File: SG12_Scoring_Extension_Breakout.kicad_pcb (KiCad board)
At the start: 2 copper layers, 100 x 100 mm, 37 parts, among them J1 RJ45, J10 Conn_01x02, J11 Conn_01x02, J12 Conn_01x02, J13 Conn_01x02, J14 Conn_01x02, J15 Conn_01x02, J16 Conn_02x04_Top_Bottom, J17 Conn_02x04_Top_Bottom, J18 Conn_02x04_Top_Bottom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

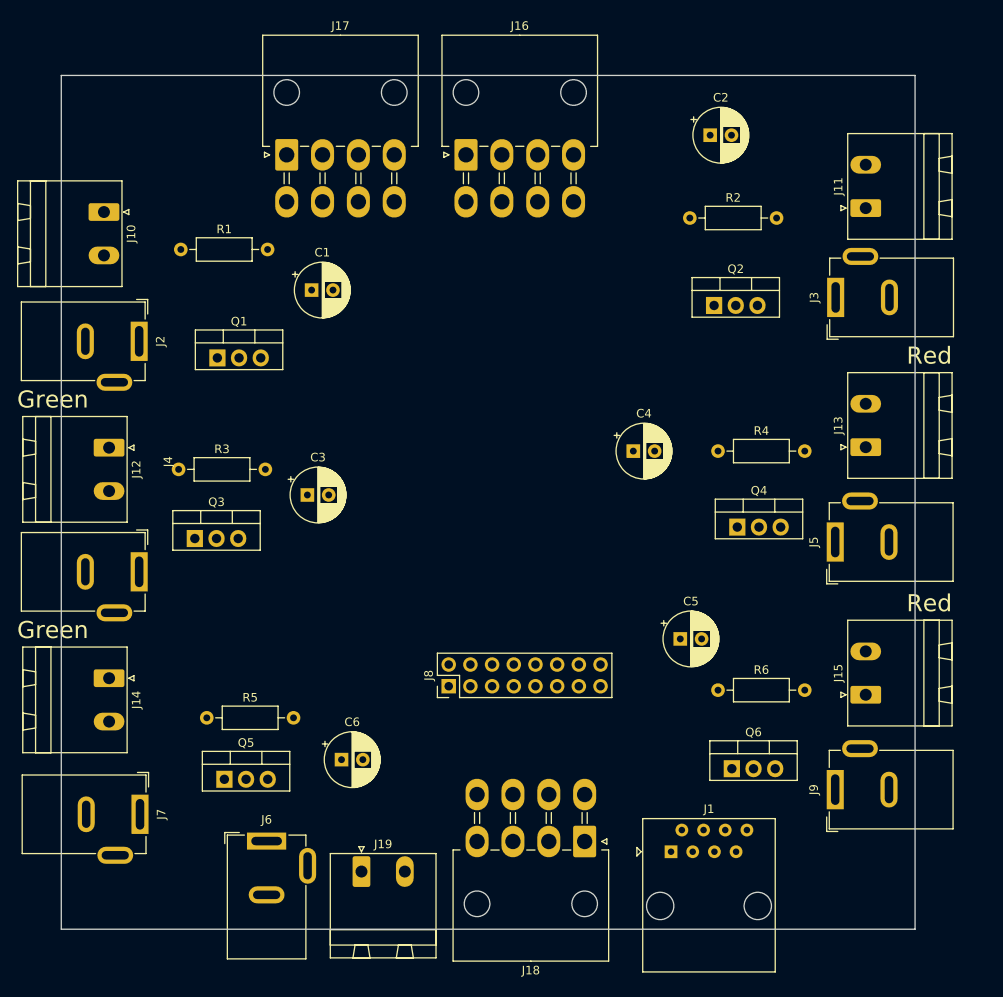
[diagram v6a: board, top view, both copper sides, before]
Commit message: Added mouting holes, iteration 2
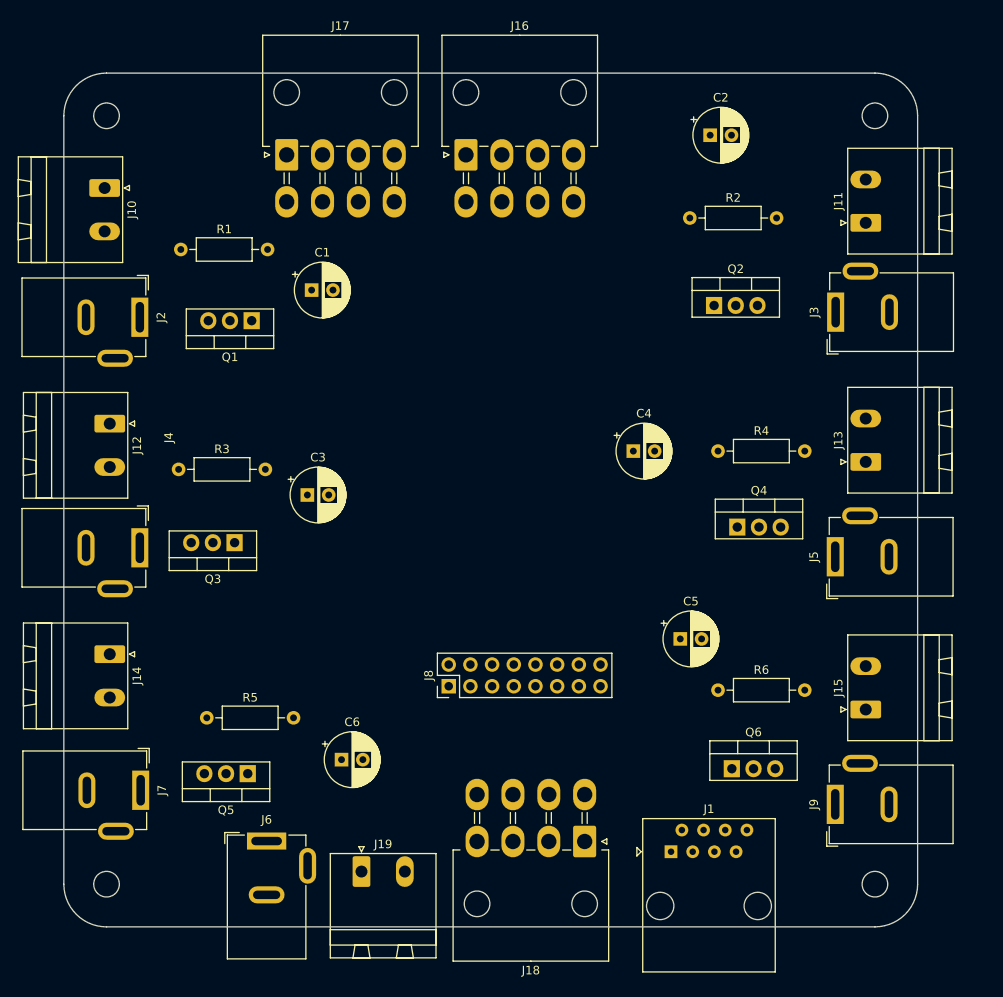
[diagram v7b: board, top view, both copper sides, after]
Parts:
- added REF**: MountingHole_3mm, MountingHole:MountingHole_3mm, F.Cu at (198.0, 53.0)
- added REF**: MountingHole_3mm, MountingHole:MountingHole_3mm, F.Cu at (108.0, 53.0)
- added REF**: MountingHole_3mm, MountingHole:MountingHole_3mm, F.Cu at (108.0, 143.0)
- added REF**: MountingHole_3mm, MountingHole:MountingHole_3mm, F.Cu at (198.0, 143.0)
- moved Q1 5.93 mm to (125.0, 77.0), turned to 180 degrees
- moved Q3 4.68 mm to (123.0, 103.0), turned to 180 degrees
- moved J2 2.82 mm to (111.9, 76.6)
- moved J4 2.82 mm to (111.9, 103.6)
- moved J10 2.82 mm to (107.8, 61.5)
- moved J12 2.82 mm to (108.4, 89.1)
- moved J14 2.82 mm to (108.4, 116.1)
- moved J7 2.82 mm to (112.0, 132.0)
- moved Q5 2.82 mm to (124.5, 130.1), turned to 180 degrees
- moved J11 1.73 mm to (196.9, 65.5)
- moved J13 1.73 mm to (196.9, 93.5)
- moved J15 1.73 mm to (196.9, 122.5)
- moved J5 1.73 mm to (193.3, 104.7)
- moved J3 1.72 mm to (193.4, 76.0)
- moved J9 1.72 mm to (193.3, 133.7)
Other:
- outline, holes or cut-outs redrawn
- board text removed: "Green"
- board text removed: "Red"

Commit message: Flipped connections on mini-fit connectors to match EPS12V
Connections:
- J16 pad 1: /Green_PullUp -> GND
- J16 pad 2: /Red_PullUp -> GND
- J16 pad 3: /WhiteG_PullUp -> GND
- J16 pad 4: /WhiteR_PullUp -> GND
- J16 pad 5: GND -> /Green_PullUp
- J16 pad 6: GND -> /Red_PullUp
- J16 pad 7: GND -> /WhiteG_PullUp
- J16 pad 8: GND -> /WhiteR_PullUp
- J17 pad 1: /Green_PullUp -> GND
- J17 pad 2: /Red_PullUp -> GND
- J17 pad 3: /WhiteG_PullUp -> GND
- J17 pad 4: /WhiteR_PullUp -> GND
- J17 pad 5: GND -> /Green_PullUp
- J17 pad 6: GND -> /Red_PullUp
- J17 pad 7: GND -> /WhiteG_PullUp
- J17 pad 8: GND -> /WhiteR_PullUp
- J18 pad 1: +12V -> GND
- J18 pad 2: +12V -> GND
- J18 pad 3: +12V -> GND
- J18 pad 4: +12V -> GND
- J18 pad 5: GND -> +12V
- J18 pad 6: GND -> +12V
- J18 pad 7: GND -> +12V
- J18 pad 8: GND -> +12V
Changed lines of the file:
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@@
     (pad "" np_thru_hole circle (at 12.6 -7.3) (size 3 3) (drill 3) (layers "*.Cu" "*.Mask"))
     (pad "1" thru_hole roundrect (at 0 0) (size 2.7 3.7) (drill 1.8) (layers "*.Cu" "*.Mask") (roundrect_rratio 0.092593)
-      (net 9 "/Green_PullUp") (pinfunction "Pin_1") (pintype "passive"))
+      (net 2 "GND") (pinfunction "Pin_1") (pintype "passive"))
     (pad "2" thru_hole oval (at 4.2 0) (size 2.7 3.7) (drill 1.8) (layers "*.Cu" "*.Mask")
-      (net 10 "/Red_PullUp") (pinfunction "Pin_2") (pintype "passive"))
+      (net 2 "GND") (pinfunction "Pin_2") (pintype "passive"))
     (pad "3" thru_hole oval (at 8.4 0) (size 2.7 3.7) (drill 1.8) (layers "*.Cu" "*.Mask")
-      (net 11 "/WhiteG_PullUp") (pinfunction "Pin_3") (pintype "passive"))
+      (net 2 "GND") (pinfunction "Pin_3") (pintype "passive"))
     (pad "4" thru_hole oval (at 12.6 0) (size 2.7 3.7) (drill 1.8) (layers "*.Cu" "*.Mask")
-      (net 12 "/WhiteR_PullUp") (pinfunction "Pin_4") (pintype "passive"))
+      (net 2 "GND") (pinfunction "Pin_4") (pintype "passive"))
     (pad "5" thru_hole oval (at 0 5.5) (size 2.7 3.7) (drill 1.8) (layers "*.Cu" "*.Mask")
-      (net 2 "GND") (pinfunction "Pin_5") (pintype "passive"))
+      (net 9 "/Green_PullUp") (pinfunction "Pin_5") (pintype "passive"))
     (pad "6" thru_hole oval (at 4.2 5.5) (size 2.7 3.7) (drill 1.8) (layers "*.Cu" "*.Mask")
-      (net 2 "GND") (pinfunction "Pin_6") (pintype "passive"))
+      (net 10 "/Red_PullUp") (pinfunction "Pin_6") (pintype "passive"))
     (pad "7" thru_hole oval (at 8.4 5.5) (size 2.7 3.7) (drill 1.8) (layers "*.Cu" "*.Mask")
-      (net 2 "GND") (pinfunction "Pin_7") (pintype "passive"))
+      (net 11 "/WhiteG_PullUp") (pinfunction "Pin_7") (pintype "passive"))
     (pad "8" thru_hole oval (at 12.6 5.5) (size 2.7 3.7) (drill 1.8) (layers "*.Cu" "*.Mask")
-      (net 2 "GND") (pinfunction "Pin_8") (pintype "passive"))
+      (net 12 "/WhiteR_PullUp") (pinfunction "Pin_8") (pintype "passive"))
     (model "${KICAD6_3DMODEL_DIR}/Connector_Molex.3dshapes/Molex_Mini-Fit_Jr_5569-08A2_2x04_P4.20mm_Horizontal.wrl"
       (offset (xyz 0 0 0))
@@
     (pad "" np_thru_hole circle (at 12.6 -7.3) (size 3 3) (drill 3) (layers "*.Cu" "*.Mask"))
     (pad "1" thru_hole roundrect (at 0 0) (size 2.7 3.7) (drill 1.8) (layers "*.Cu" "*.Mask") (roundrect_rratio 0.092593)
-      (net 9 "/Green_PullUp") (pinfunction "Pin_1") (pintype "passive"))
+      (net 2 "GND") (pinfunction "Pin_1") (pintype "passive"))
     (pad "2" thru_hole oval (at 4.2 0) (size 2.7 3.7) (drill 1.8) (layers "*.Cu" "*.Mask")
-      (net 10 "/Red_PullUp") (pinfunction "Pin_2") (pintype "passive"))
+      (net 2 "GND") (pinfunction "Pin_2") (pintype "passive"))
     (pad "3" thru_hole oval (at 8.4 0) (size 2.7 3.7) (drill 1.8) (layers "*.Cu" "*.Mask")
-      (net 11 "/WhiteG_PullUp") (pinfunction "Pin_3") (pintype "passive"))
+      (net 2 "GND") (pinfunction "Pin_3") (pintype "passive"))
     (pad "4" thru_hole oval (at 12.6 0) (size 2.7 3.7) (drill 1.8) (layers "*.Cu" "*.Mask")
-      (net 12 "/WhiteR_PullUp") (pinfunction "Pin_4") (pintype "passive"))
+      (net 2 "GND") (pinfunction "Pin_4") (pintype "passive"))
     (pad "5" thru_hole oval (at 0 5.5) (size 2.7 3.7) (drill 1.8) (layers "*.Cu" "*.Mask")
-      (net 2 "GND") (pinfunction "Pin_5") (pintype "passive"))
+      (net 9 "/Green_PullUp") (pinfunction "Pin_5") (pintype "passive"))
     (pad "6" thru_hole oval (at 4.2 5.5) (size 2.7 3.7) (drill 1.8) (layers "*.Cu" "*.Mask")
-      (net 2 "GND") (pinfunction "Pin_6") (pintype "passive"))
+      (net 10 "/Red_PullUp") (pinfunction "Pin_6") (pintype "passive"))
     (pad "7" thru_hole oval (at 8.4 5.5) (size 2.7 3.7) (drill 1.8) (layers "*.Cu" "*.Mask")
-      (net 2 "GND") (pinfunction "Pin_7") (pintype "passive"))
+      (net 11 "/WhiteG_PullUp") (pinfunction "Pin_7") (pintype "passive"))
     (pad "8" thru_hole oval (at 12.6 5.5) (size 2.7 3.7) (drill 1.8) (layers "*.Cu" "*.Mask")
-      (net 2 "GND") (pinfunction "Pin_8") (pintype "passive"))
+      (net 12 "/WhiteR_PullUp") (pinfunction "Pin_8") (pintype "passive"))
     (model "${KICAD6_3DMODEL_DIR}/Connector_Molex.3dshapes/Molex_Mini-Fit_Jr_5569-08A2_2x04_P4.20mm_Horizontal.wrl"
       (offset (xyz 0 0 0))
@@
     (pad "" np_thru_hole circle (at 12.6 -7.3 180) (size 3 3) (drill 3) (layers "*.Cu" "*.Mask"))
     (pad "1" thru_hole roundrect (at 0 0 180) (size 2.7 3.7) (drill 1.8) (layers "*.Cu" "*.Mask") (roundrect_rratio 0.092593)
-      (net 1 "+12V") (pinfunction "Pin_1") (pintype "passive"))
+      (net 2 "GND") (pinfunction "Pin_1") (pintype "passive"))
     (pad "2" thru_hole oval (at 4.2 0 180) (size 2.7 3.7) (drill 1.8) (layers "*.Cu" "*.Mask")
-      (net 1 "+12V") (pinfunction "Pin_2") (pintype "passive"))
+      (net 2 "GND") (pinfunction "Pin_2") (pintype "passive"))
     (pad "3" thru_hole oval (at 8.4 0 180) (size 2.7 3.7) (drill 1.8) (layers "*.Cu" "*.Mask")
-      (net 1 "+12V") (pinfunction "Pin_3") (pintype "passive"))
+      (net 2 "GND") (pinfunction "Pin_3") (pintype "passive"))
     (pad "4" thru_hole oval (at 12.6 0 180) (size 2.7 3.7) (drill 1.8) (layers "*.Cu" "*.Mask")
-      (net 1 "+12V") (pinfunction "Pin_4") (pintype "passive"))
+      (net 2 "GND") (pinfunction "Pin_4") (pintype "passive"))
     (pad "5" thru_hole oval (at 0 5.5 180) (size 2.7 3.7) (drill 1.8) (layers "*.Cu" "*.Mask")
-      (net 2 "GND") (pinfunction "Pin_5") (pintype "passive"))
+      (net 1 "+12V") (pinfunction "Pin_5") (pintype "passive"))
     (pad "6" thru_hole oval (at 4.2 5.5 180) (size 2.7 3.7) (drill 1.8) (layers "*.Cu" "*.Mask")
-      (net 2 "GND") (pinfunction "Pin_6") (pintype "passive"))
+      (net 1 "+12V") (pinfunction "Pin_6") (pintype "passive"))
     (pad "7" thru_hole oval (at 8.4 5.5 180) (size 2.7 3.7) (drill 1.8) (layers "*.Cu" "*.Mask")
-      (net 2 "GND") (pinfunction "Pin_7") (pintype "passive"))
+      (net 1 "+12V") (pinfunction "Pin_7") (pintype "passive"))
     (pad "8" thru_hole oval (at 12.6 5.5 180) (size 2.7 3.7) (drill 1.8) (layers "*.Cu" "*.Mask")
-      (net 2 "GND") (pinfunction "Pin_8") (pintype "passive"))
+      (net 1 "+12V") (pinfunction "Pin_8") (pintype "passive"))
     (model "${KICAD6_3DMODEL_DIR}/Connector_Molex.3dshapes/Molex_Mini-Fit_Jr_5569-08A2_2x04_P4.20mm_Horizontal.wrl"
       (offset (xyz 0 0 0))
